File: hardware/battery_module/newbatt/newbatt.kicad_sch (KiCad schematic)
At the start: 33 parts, among them J1 DC050-T, J2 Conn_01x05_Pin, U1 BQ24210DQCR, U5 XC6210B332MR

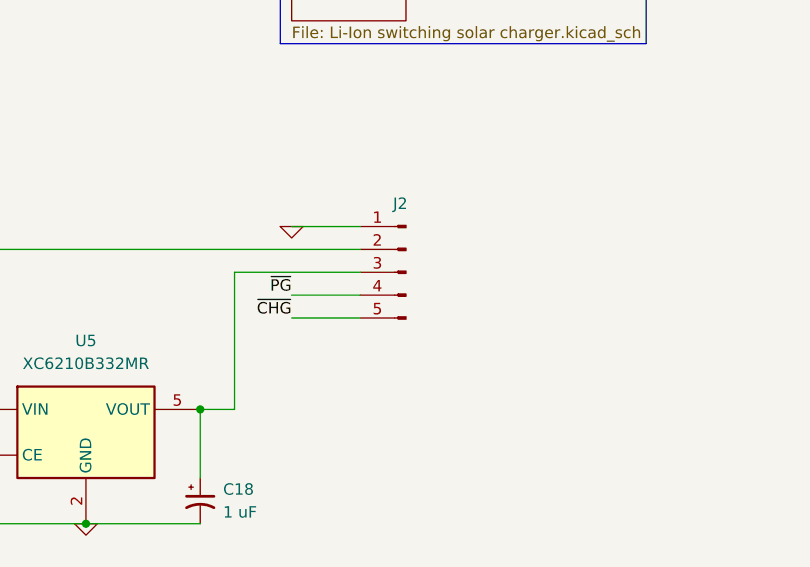
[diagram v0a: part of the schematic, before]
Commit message: JST PH --> JST SH
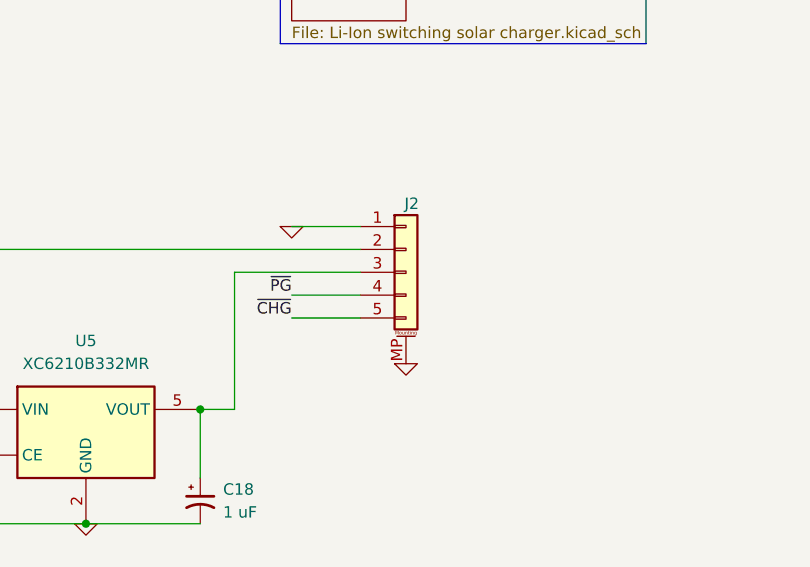
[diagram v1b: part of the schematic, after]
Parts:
- J2: value Conn_01x05_Pin -> Conn_01x05_MountingPin; footprint Connector_JST:JST_PH_S5B-PH-SM4-TB_1x05-1MP_P2.00mm_Horizontal -> Connector_JST:JST_SH_SM05B-SRSS-TB_1x05-1MP_P1.00mm_Horizontal; symbol Connector:Conn_01x05_Pin -> Connector_Generic_MountingPin:Conn_01x05_MountingPin; Digikey S5485-ND -> 455-SM05B-SRSS-TBCT-ND; LCSC C7327804 -> C136657; MFC Sullins Connector Solutions -> JST; MPN PPPC101LGBN-RC -> SM05B-SRSS-TB
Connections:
- net 0: now also J2.MP (MountPin)
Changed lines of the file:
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@@
 	)
 	(symbol
-		(lib_id "Connector:Conn_01x05_Pin")
+		(lib_id "Connector_Generic_MountingPin:Conn_01x05_MountingPin")
 		(at 234.95 71.12 0)
-		(mirror y)
 		(unit 1)
 		(exclude_from_sim no)
@@
 		(dnp no)
 		(property "Reference" "J2"
-			(at 234.315 63.5 0)
-			(effects
-				(font
-					(size 1.27 1.27)
-				)
-			)
-		)
-		(property "Value" "Conn_01x05_Pin"
-			(at 232.41 73.6599 0)
+			(at 235.585 63.5 0)
+			(effects
+				(font
+					(size 1.27 1.27)
+				)
+			)
+		)
+		(property "Value" "Conn_01x05_MountingPin"
+			(at 237.49 73.6599 0)
 			(effects
 				(font
@@
 			)
 		)
-		(property "Footprint" "Connector_JST:JST_PH_S5B-PH-SM4-TB_1x05-1MP_P2.00mm_Horizontal"
+		(property "Footprint" "Connector_JST:JST_SH_SM05B-SRSS-TB_1x05-1MP_P1.00mm_Horizontal"
 			(at 234.95 71.12 0)
 			(effects
@@
 			)
 		)
-		(property "Description" "Generic connector, single row, 01x05, script generated"
+		(property "Description" "JST SH 5 pin"
 			(at 234.95 71.12 0)
 			(effects
@@
 			)
 		)
-		(property "MFC" "Sullins Connector Solutions"
+		(property "MFC" "JST"
 			(at 234.95 71.12 0)
 			(effects
@@
 			)
 		)
-		(property "MPN" "PPPC101LGBN-RC"
+		(property "MPN" "SM05B-SRSS-TB"
 			(at 234.95 71.12 0)
 			(effects
@@
 			)
 		)
-		(property "Digikey" "S5485-ND"
+		(property "Digikey" "455-SM05B-SRSS-TBCT-ND"
 			(at 234.95 71.12 0)
 			(effects
@@
 			)
 		)
-		(property "LCSC" "C7327804"
+		(property "LCSC" "C136657"
 			(at 234.95 71.12 0)
 			(effects
@@
 		)
 		(pin "5"
+		)
+		(pin "MP"
 		)
 		(instances
@@
 					(unit 1)
 				)
+			)
+		)
+	)
+	(symbol
+		(lib_id "Simulation_SPICE:0")
+		(at 234.95 81.28 0)
+		(unit 1)
+		(exclude_from_sim no)
+		(in_bom yes)
+		(on_board yes)
+		(dnp no)
+		(fields_autoplaced yes)
+		(property "Reference" "#GND012"
+			(at 234.95 86.36 0)
+			(effects
+				(font
+					(size 1.27 1.27)
+				)
+				(hide yes)
+			)
+		)
+		(property "Value" "0"
+			(at 234.95 78.74 0)
+			(effects
+				(font
+					(size 1.27 1.27)
+				)
+				(hide yes)
+			)
+		)
+		(property "Footprint" ""
+			(at 234.95 81.28 0)
+			(effects
+				(font
+					(size 1.27 1.27)
+				)
+				(hide yes)
+			)
+		)
+		(property "Datasheet" "https://ngspice.sourceforge.io/docs/ngspice-html-manual/manual.xhtml#subsec_Circuit_elements__device"
+			(at 234.95 91.44 0)
+			(effects
+				(font
+					(size 1.27 1.27)
+				)
+				(hide yes)
+			)
+		)
+		(property "Description" "0V reference potential for simulation"
+			(at 234.95 88.9 0)
+			(effects
+				(font
+					(size 1.27 1.27)
+				)
+				(hide yes)
+			)
+		)
+		(pin "1"
+		)
+		(instances
+			(project "newbatt"
+				(path "/492e8d1d-dcc5-45c6-a3d2-2dfd8a06477e"
+					(reference "#GND012")
+					(unit 1)
+				)
